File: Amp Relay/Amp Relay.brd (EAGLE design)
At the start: 57.5 x 55 mm, 17 parts, among them IC1 LM358D, J1 OSTTA024163, J2 SJ-3523-SMT-TR, J3 SJ-3523-SMT-TR, Q1 BC849SMD, U1 G5LE-1A4_DC5

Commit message: aux ground and terminal block soldermask fix
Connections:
- removed net N$7: J2.1, J3.1
- net GND: now also J2.1, J3.1
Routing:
- net GND: track 33.3 -> 47.7 mm, vias 2 -> 3
- net N$7: track 11.8 -> 0.00 mm
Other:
- board text added: "Audio Relay v1.1"
- board text removed: "Audio Relay v1.0"
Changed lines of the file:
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@@
 <text x="49.1" y="53.4" size="1.27" layer="21">PWR IN</text>
 <text x="56.8" y="0.7" size="1.27" layer="22" rot="MR0">Sean Sylwester</text>
-<text x="56.8" y="2.4" size="1.27" layer="22" rot="MR0">Audio Relay v1.0</text>
+<text x="56.8" y="2.4" size="1.27" layer="22" rot="MR0">Audio Relay v1.1</text>
 </plain>
 <attributes>
@@
 <vertex x="0.1" y="0.15"/>
 </polygon>
+<contactref element="J3" pad="1"/>
+<contactref element="J2" pad="1"/>
+<wire x1="2.4" y1="14.4" x2="1.742" y2="13.742" width="0.508" layer="1"/>
+<wire x1="1.742" y1="13.742" x2="1.742" y2="4.63749375" width="0.508" layer="1"/>
+<wire x1="1.742" y1="4.63749375" x2="2.4" y2="3.97949375" width="0.508" layer="1"/>
+<wire x1="2.4" y1="3.97949375" x2="2.4" y2="3.1" width="0.508" layer="1"/>
+<via x="5" y="3.1" extent="1-16" drill="0.3937"/>
+<wire x1="2.4" y1="3.1" x2="5" y2="3.1" width="0.508" layer="1"/>
 </signal>
 <signal name="N$3">
@@
 <wire x1="5.058" y1="11.158" x2="4.4" y2="10.5" width="0.508" layer="1"/>
 </signal>
-<signal name="N$7">
-<contactref element="J3" pad="1"/>
-<contactref element="J2" pad="1"/>
-<wire x1="2.4" y1="14.4" x2="1.742" y2="13.742" width="0.508" layer="1"/>
-<wire x1="1.742" y1="13.742" x2="1.742" y2="4.63749375" width="0.508" layer="1"/>
-<wire x1="1.742" y1="4.63749375" x2="2.4" y2="3.97949375" width="0.508" layer="1"/>
-<wire x1="2.4" y1="3.97949375" x2="2.4" y2="3.1" width="0.508" layer="1"/>
-</signal>
 <signal name="IN_N">

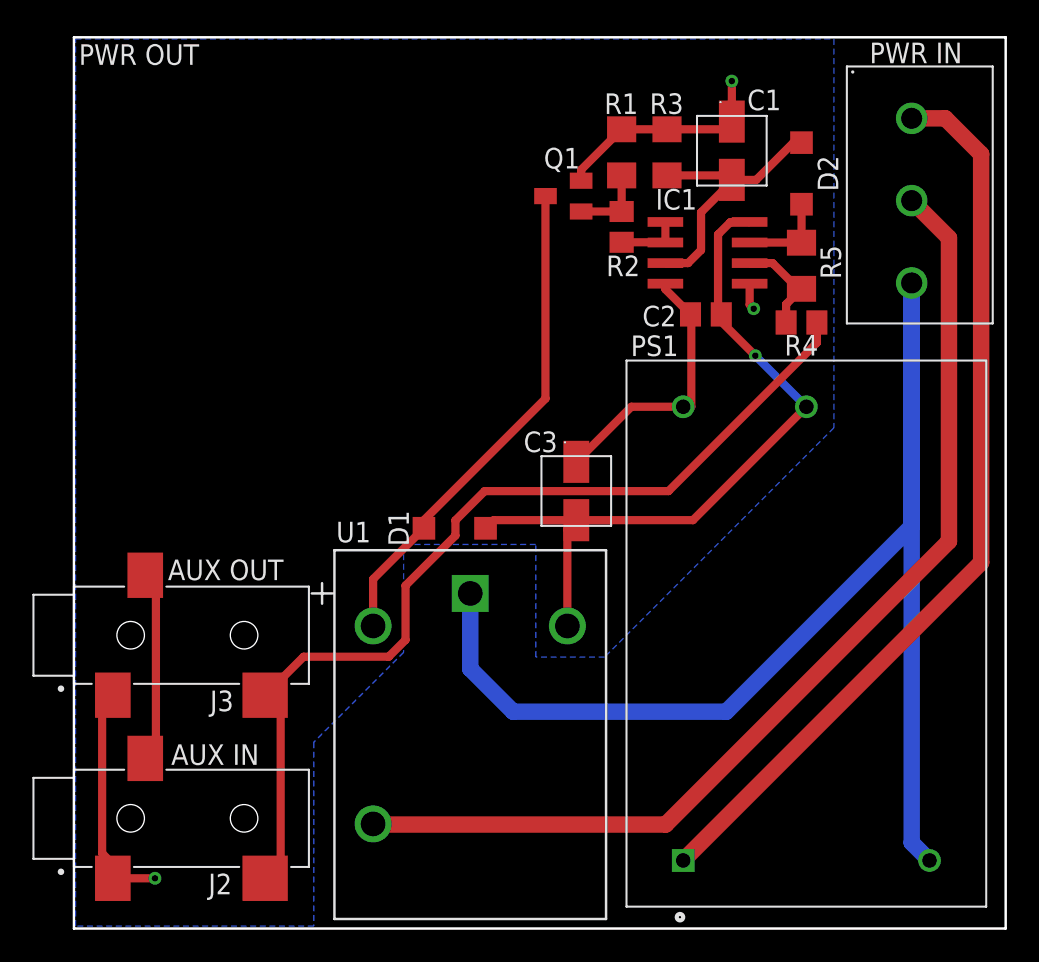
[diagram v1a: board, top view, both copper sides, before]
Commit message: added toggle switch, and cutouts for the aux ports
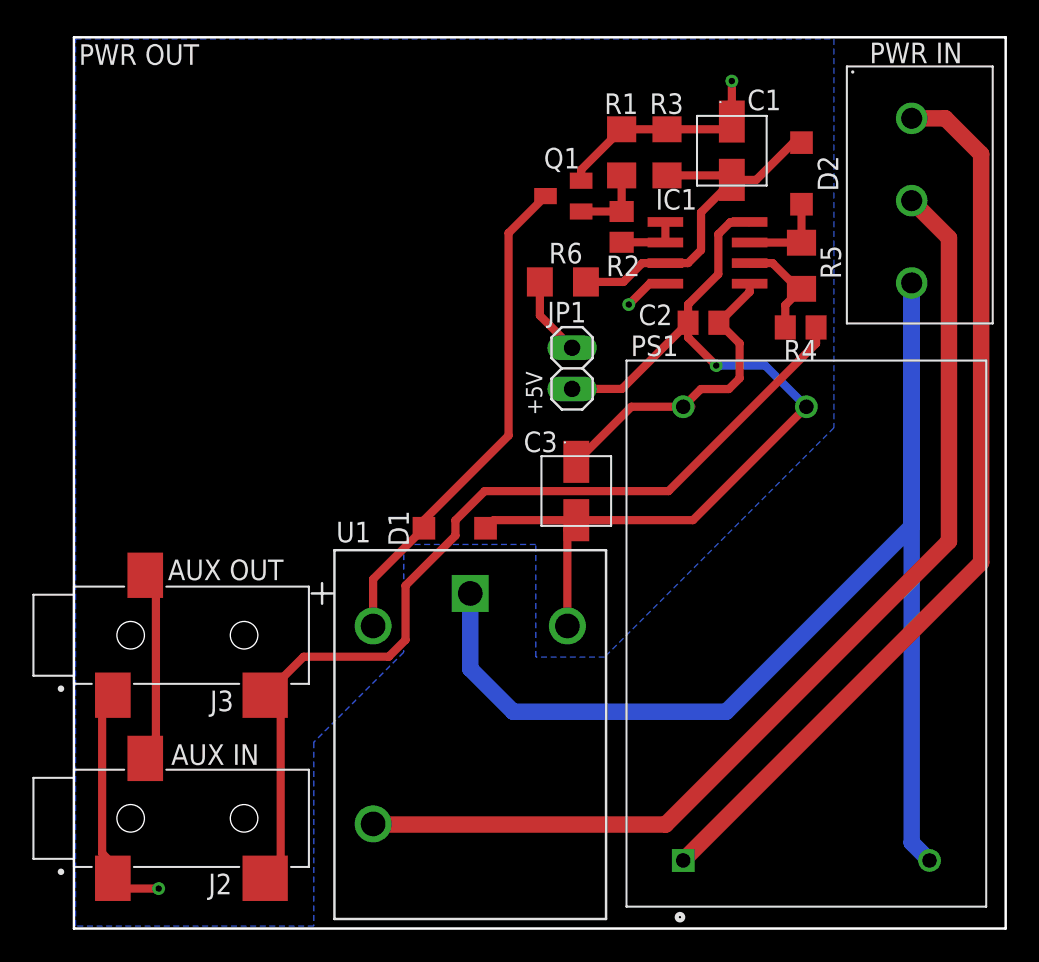
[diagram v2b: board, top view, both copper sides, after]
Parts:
- added JP1: (no value), pinhead:1X02
- added R6: 10k, rcl:R1206
- moved C2 0.54 mm to (38.9, 37.4), turned to 0 degrees
- moved R4 0.31 mm to (44.8, 37.1)
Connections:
- new net N$1: JP1.2, R6.2
- net N$5: now also R6.1
- net VCC: now also JP1.1
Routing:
- net VCC: track 44.8 -> 57.0 mm
- net N$5: track 17.1 -> 22.4 mm
- net N$1: track 0.00 -> 4.88 mm
- net GND: track 47.7 -> 52.0 mm
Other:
- board text added: "+5V"
